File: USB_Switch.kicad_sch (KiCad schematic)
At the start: 2 parts, among them J1 Conn_01x06, J4 Conn_01x08

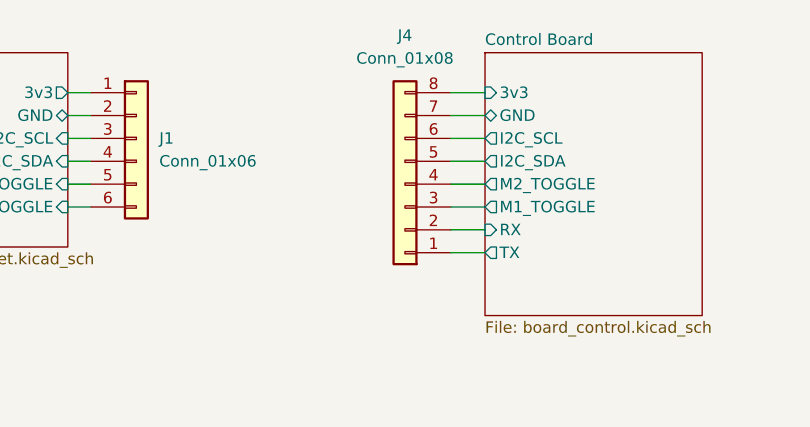
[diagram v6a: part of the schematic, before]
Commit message: Fixed inversed naming on connectors
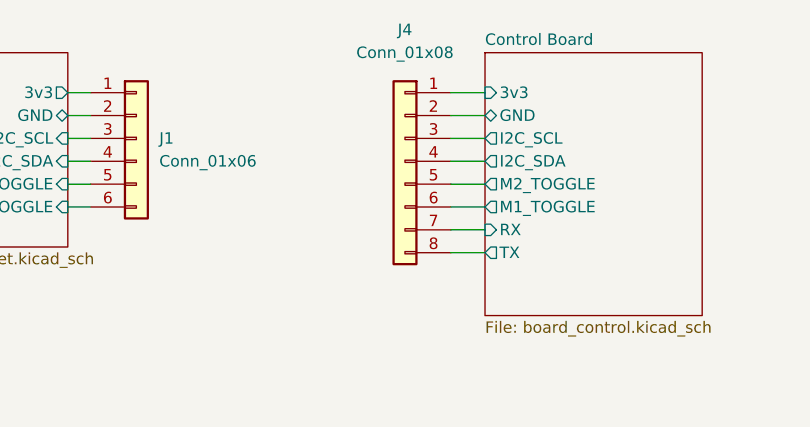
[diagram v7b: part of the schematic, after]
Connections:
- net Control Board/3v3: now also J4.1 (Pin_1); no longer J4.8 (Pin_8)
- net Control Board/GND: now also J4.2 (Pin_2); no longer J4.7 (Pin_7)
- net Control Board/I2C_SCL: now also J4.3 (Pin_3); no longer J4.6 (Pin_6)
- net Control Board/I2C_SDA: now also J4.4 (Pin_4); no longer J4.5 (Pin_5)
- net Control Board/M1_TOGGLE: now also J4.6 (Pin_6); no longer J4.3 (Pin_3)
- net Control Board/M2_TOGGLE: now also J4.5 (Pin_5); no longer J4.4 (Pin_4)
- net Control Board/RX: now also J4.7 (Pin_7); no longer J4.2 (Pin_2)
- net Control Board/TX: now also J4.8 (Pin_8); no longer J4.1 (Pin_1)
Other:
- moved on the sheet: J4
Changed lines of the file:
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@@
     (effects (font (size 1.27 1.27)) (justify left bottom))
   )
-  (symbol (lib_id "Connector_Generic:Conn_01x08") (at 132.715 59.055 180) (unit 1)
+  (symbol (lib_id "Connector_Generic:Conn_01x08") (at 132.715 56.515 0) (mirror y) (unit 1)
     (in_bom yes) (on_board yes) (fields_autoplaced)
-    (property "Reference" "J4" (id 0) (at 132.715 42.545 0))
-    (property "Value" "Conn_01x08" (id 1) (at 132.715 45.085 0))
-    (property "Footprint" "Connector_PinHeader_2.54mm:PinHeader_1x08_P2.54mm_Vertical" (id 2) (at 132.715 59.055 0)
+    (property "Reference" "J4" (id 0) (at 132.715 41.91 0))
+    (property "Value" "Conn_01x08" (id 1) (at 132.715 44.45 0))
+    (property "Footprint" "Connector_PinHeader_2.54mm:PinHeader_1x08_P2.54mm_Vertical" (id 2) (at 132.715 56.515 0)
       (effects (font (size 1.27 1.27)) hide)
     )
-    (property "Datasheet" "~" (id 3) (at 132.715 59.055 0)
+    (property "Datasheet" "~" (id 3) (at 132.715 56.515 0)
       (effects (font (size 1.27 1.27)) hide)
     )

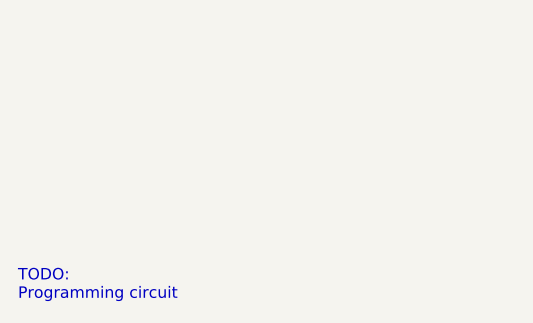
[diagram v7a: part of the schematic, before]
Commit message: Added more GND vias, fixed incorrect net trace sizing
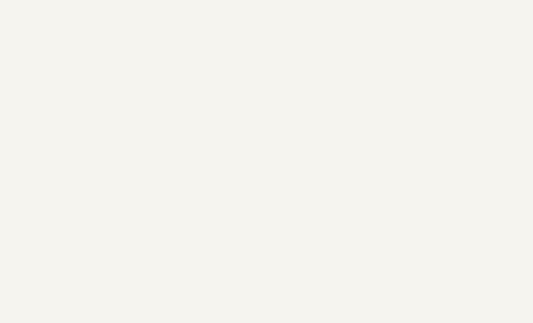
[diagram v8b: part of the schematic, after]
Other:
- note removed: "TODO: Programming circuit"
- title: (none) -> Smart USB Port
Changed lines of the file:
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@@
 (kicad_sch (version 20211123) (generator eeschema)
   (paper "A4")
+  (title_block
+    (title "Smart USB Port")
+    (date "2022-10-23")
+    (rev "0.1")
+  )
   (wire (pts (xy 137.795 48.895) (xy 141.605 48.895))
     (stroke (width 0) (type default) (color 0 0 0 0))
@@
     (stroke (width 0) (type default) (color 0 0 0 0))
   )
-  (text "TODO:\nProgramming circuit" (at 40.64 139.7 0)
-    (effects (font (size 1.27 1.27)) (justify left bottom))
-  )
   (symbol (lib_id "Connector_Generic:Conn_01x08") (at 132.715 56.515 0) (mirror y) (unit 1)
